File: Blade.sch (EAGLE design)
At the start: 162 parts, among them IC1 THN10-2411WIR, IC10 MCP6064-E/SL, IC2 MCP6064-E/SL, IC3 MCP6064-E/SL, IC4 MCP6064-E/SL, IC5 MAX488CSA, IC6 MOCD207MSOIC-8, IC7 MOCD207MSOIC-8, IC8 MOCD207MSOIC-8, IC9 MCP6064-E/SL, Q1 12MHz, U1 ADR366WAUJZ, U10 ADS1148QPWRQ1, U11 ADS1148QPWRQ1, U12 ADS1148QPWRQ1, U2 ADR366WAUJZ, U3 ADS1148QPWRQ1, U4 ADS1148QPWRQ1, U5 ADS1148QPWRQ1, U6 LT1528, U7 S70FL01GS, U8 S70FL01GS, U9 STM32F77XXXLQFP208, X1 D-SUB9-H5M09RA, X2 D-SUB15-H5M15RA, X3 USBPTH

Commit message: rerouting
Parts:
- added C52: 10n, rcl:C-EUC0805
- added R22: 100k, rcl:R-EU_R0805
- added R23: 1k, rcl:R-EU_R0805
- added R24, R25: ?, rcl:R-EU_R0805
- added U13: ADR366WAUJZ, ADR360:ADR36_UJZ
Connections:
- new net 3V3REF3: R24.2, U13.VOUT, U9.VREF+
- new net ADC4_DRDY: U11.!DRDY, U9.PH0
- new net ADC4_RES: U11.!RESET, U9.PF10
- new net ADC4_START: U11.START, U9.PF9
- new net ADC5_DRDY: U10.!DRDY, U9.PA1
- new net ADC5_RES: U10.!RESET, U9.PC2
- new net ADC5_START: U10.START, U9.PC0
- new net ADC6_DRDY: U12.!DRDY, U9.PA2
- new net ADC6_RES: U12.!RESET, U9.PH1
- new net ADC6_START: U12.START, U9.PC3
- new net N$68: R22.1, U13.TRIM
- new net N$69: R22.2, R24.1, R25.2
- new net N$70: R23.2, R25.1
- net 3V3REF2: no longer U9.VREF+
- net 5V: now also C52.2, U13.VIN
- net ADC1_DRDY: no longer U11.!DRDY
- net ADC1_RES: no longer U11.!RESET
- net ADC1_START: no longer U11.START
- net ADC2_DRDY: no longer U10.!DRDY
- net ADC2_RES: no longer U10.!RESET
- net ADC2_START: no longer U10.START
- net ADC3_DRDY: no longer U12.!DRDY
- net ADC3_RES: no longer U12.!RESET
- net ADC3_START: no longer U12.START
- net GND: now also C52.1, R23.1, U13.GND

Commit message: bom added, text cleanup
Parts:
- renumbered SV1 to X_PROG, U$1 to IC12, U$2 to IC13
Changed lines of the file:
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@@
 <part name="X1" library="con-thomas-betts" library_urn="urn:adsk.eagle:library:191" deviceset="D-SUB9-" device="H5M09RA" package3d_urn="urn:adsk.eagle:package:10559/1"/>
 <part name="X3" library="aSparkFun" deviceset="USB" device="PTH"/>
-<part name="SV1" library="con-lstb" library_urn="urn:adsk.eagle:library:162" deviceset="MA07-2" device="" package3d_urn="urn:adsk.eagle:package:8330/1"/>
-<part name="U$2" library="ch340g" deviceset="CH340G" device=""/>
+<part name="X_PROG" library="con-lstb" library_urn="urn:adsk.eagle:library:162" deviceset="MA07-2" device="" package3d_urn="urn:adsk.eagle:package:8330/1"/>
+<part name="IC13" library="ch340g" deviceset="CH340G" device=""/>
 <part name="Q1" library="adafruit" deviceset="CRYSTAL" device="SM49" value="12MHz"/>
 <part name="C1" library="rcl" deviceset="C-EU" device="C0603" value="22p"/>
@@
 <part name="D8" library="diodes" deviceset="DZ" device="MELF" value="3V6"/>
 <part name="D9" library="diodes" deviceset="DZ" device="MELF" value="3V6"/>
-<part name="U$1" library="m-pad-2.1" deviceset="LM78L05ACMX/NOPB" device=""/>
+<part name="IC12" library="m-pad-2.1" deviceset="LM78L05ACMX/NOPB" device=""/>
 <part name="C42" library="rcl" library_urn="urn:adsk.eagle:library:334" deviceset="C-EU" device="C0805" package3d_urn="urn:adsk.eagle:package:23617/2" value="100n"/>
 <part name="C43" library="rcl" library_urn="urn:adsk.eagle:library:334" deviceset="C-EU" device="C0805" package3d_urn="urn:adsk.eagle:package:23617/2" value="100n"/>
@@
 </instance>
 <instance part="X3" gate="G$1" x="101.6" y="93.98" smashed="yes" rot="R180"/>
-<instance part="SV1" gate="G$1" x="160.02" y="116.84" smashed="yes" rot="R180">
+<instance part="X_PROG" gate="G$1" x="160.02" y="116.84" smashed="yes" rot="R180">
 <attribute name="VALUE" x="163.83" y="129.54" size="1.778" layer="96" rot="R180"/>
 <attribute name="NAME" x="163.83" y="105.918" size="1.778" layer="95" rot="R180"/>
@@
 </segment>
 <segment>
-<pinref part="SV1" gate="G$1" pin="14"/>
+<pinref part="X_PROG" gate="G$1" pin="14"/>
 <wire x1="167.64" y1="109.22" x2="172.72" y2="109.22" width="0.1524" layer="91"/>
 <wire x1="172.72" y1="109.22" x2="172.72" y2="114.3" width="0.1524" layer="91"/>
-<pinref part="SV1" gate="G$1" pin="2"/>
+<pinref part="X_PROG" gate="G$1" pin="2"/>
 <wire x1="172.72" y1="114.3" x2="172.72" y2="116.84" width="0.1524" layer="91"/>
 <wire x1="172.72" y1="116.84" x2="172.72" y2="119.38" width="0.1524" layer="91"/>
@@
 <wire x1="172.72" y1="124.46" x2="167.64" y2="124.46" width="0.1524" layer="91"/>
 <label x="172.72" y="124.46" size="1.27" layer="95" xref="yes"/>
-<pinref part="SV1" gate="G$1" pin="4"/>
+<pinref part="X_PROG" gate="G$1" pin="4"/>
 <wire x1="167.64" y1="121.92" x2="172.72" y2="121.92" width="0.1524" layer="91"/>
 <junction x="172.72" y="121.92"/>
-<pinref part="SV1" gate="G$1" pin="6"/>
+<pinref part="X_PROG" gate="G$1" pin="6"/>
 <wire x1="172.72" y1="119.38" x2="167.64" y2="119.38" width="0.1524" layer="91"/>
 <junction x="172.72" y="119.38"/>
-<pinref part="SV1" gate="G$1" pin="8"/>
+<pinref part="X_PROG" gate="G$1" pin="8"/>
 <wire x1="167.64" y1="116.84" x2="172.72" y2="116.84" width="0.1524" layer="91"/>
 <junction x="172.72" y="116.84"/>
-<pinref part="SV1" gate="G$1" pin="10"/>
+<pinref part="X_PROG" gate="G$1" pin="10"/>
 <wire x1="167.64" y1="114.3" x2="172.72" y2="114.3" width="0.1524" layer="91"/>
 <junction x="172.72" y="114.3"/>
@@
 </segment>
 <segment>
-<pinref part="SV1" gate="G$1" pin="7"/>
+<pinref part="X_PROG" gate="G$1" pin="7"/>
 <wire x1="149.86" y1="116.84" x2="152.4" y2="116.84" width="0.1524" layer="91"/>
 <label x="149.86" y="116.84" size="1.27" layer="95" rot="R180" xref="yes"/>
@@
 </segment>
 <segment>
-<pinref part="SV1" gate="G$1" pin="9"/>
+<pinref part="X_PROG" gate="G$1" pin="9"/>
 <wire x1="149.86" y1="114.3" x2="152.4" y2="114.3" width="0.1524" layer="91"/>
 <label x="149.86" y="114.3" size="1.27" layer="95" rot="R180" xref="yes"/>
@@
 </segment>
 <segment>
-<pinref part="SV1" gate="G$1" pin="11"/>
+<pinref part="X_PROG" gate="G$1" pin="11"/>
 <wire x1="149.86" y1="111.76" x2="152.4" y2="111.76" width="0.1524" layer="91"/>
 <label x="149.86" y="111.76" size="1.27" layer="95" rot="R180" xref="yes"/>
@@
 </segment>
 <segment>
-<pinref part="SV1" gate="G$1" pin="3"/>
+<pinref part="X_PROG" gate="G$1" pin="3"/>
 <wire x1="149.86" y1="121.92" x2="152.4" y2="121.92" width="0.1524" layer="91"/>
 <label x="149.86" y="121.92" size="1.27" layer="95" rot="R180" xref="yes"/>
@@
 <net name="3V3" class="0">
 <segment>
-<pinref part="SV1" gate="G$1" pin="1"/>
+<pinref part="X_PROG" gate="G$1" pin="1"/>
 <wire x1="152.4" y1="124.46" x2="149.86" y2="124.46" width="0.1524" layer="91"/>
 <label x="149.86" y="124.46" size="1.27" layer="95" rot="R180" xref="yes"/>
@@
 <net name="TDI" class="0">
 <segment>
-<pinref part="SV1" gate="G$1" pin="5"/>
+<pinref part="X_PROG" gate="G$1" pin="5"/>
 <wire x1="149.86" y1="119.38" x2="152.4" y2="119.38" width="0.1524" layer="91"/>
 <label x="149.86" y="119.38" size="1.27" layer="95" rot="R180" xref="yes"/>
@@
 <net name="N$8" class="0">
 <segment>
-<pinref part="SV1" gate="G$1" pin="13"/>
+<pinref part="X_PROG" gate="G$1" pin="13"/>
 <wire x1="149.86" y1="109.22" x2="152.4" y2="109.22" width="0.1524" layer="91"/>
 </segment>
@@
 <net name="N$13" class="0">
 <segment>
-<pinref part="SV1" gate="G$1" pin="12"/>
+<pinref part="X_PROG" gate="G$1" pin="12"/>
 <wire x1="170.18" y1="111.76" x2="167.64" y2="111.76" width="0.1524" layer="91"/>
 </segment>
@@
 </plain>
 <instances>
-<instance part="U$2" gate="G$1" x="358.14" y="45.72" smashed="yes"/>
+<instance part="IC13" gate="G$1" x="358.14" y="45.72" smashed="yes"/>
 <instance part="Q1" gate="G$1" x="337.82" y="22.86" smashed="yes">
 <attribute name="NAME" x="340.36" y="23.876" size="1.778" layer="95"/>
@@
 <attribute name="VALUE" x="437.8325" y="267.335" size="1.524" layer="96" rot="R90"/>
 </instance>
-<instance part="U$1" gate="G$1" x="487.934" y="210.566" smashed="yes"/>
+<instance part="IC12" gate="G$1" x="487.934" y="210.566" smashed="yes"/>
 <instance part="C42" gate="G$1" x="480.314" y="192.786" smashed="yes" rot="R270">
 <attribute name="NAME" x="480.695" y="191.262" size="1.778" layer="95" rot="R270"/>
@@
 <net name="DAPI_P" class="0">
 <segment>
-<pinref part="U$2" gate="G$1" pin="D+"/>
+<pinref part="IC13" gate="G$1" pin="D+"/>
 <wire x1="345.44" y1="45.72" x2="312.42" y2="45.72" width="0.1524" layer="91"/>
 <label x="317.5" y="45.72" size="1.27" layer="95" rot="R270" xref="yes"/>
@@
 <net name="DAPI_N" class="0">
 <segment>
-<pinref part="U$2" gate="G$1" pin="D-"/>
+<pinref part="IC13" gate="G$1" pin="D-"/>
 <wire x1="345.44" y1="43.18" x2="322.58" y2="43.18" width="0.1524" layer="91"/>
 <label x="328.93" y="42.926" size="1.27" layer="95" rot="R270" xref="yes"/>
@@
 <net name="DAPI_RX" class="0">
 <segment>
-<pinref part="U$2" gate="G$1" pin="TX"/>
+<pinref part="IC13" gate="G$1" pin="TX"/>
 <label x="330.2" y="53.34" size="1.27" layer="95" rot="R90" xref="yes"/>
 <pinref part="D4" gate="G$1" pin="C"/>
@@
 <net name="GND" class="0">
 <segment>
-<pinref part="U$2" gate="G$1" pin="GND"/>
+<pinref part="IC13" gate="G$1" pin="GND"/>
 <wire x1="345.44" y1="55.88" x2="342.9" y2="55.88" width="0.1524" layer="91"/>
 <label x="342.9" y="55.88" size="1.27" layer="95" rot="R90" xref="yes"/>
@@
 <net name="3V3" class="0">
 <segment>
-<pinref part="U$2" gate="G$1" pin="VCC"/>
+<pinref part="IC13" gate="G$1" pin="VCC"/>
 <wire x1="370.84" y1="55.88" x2="373.38" y2="55.88" width="0.1524" layer="91"/>
 <label x="373.38" y="55.88" size="1.27" layer="95" rot="R90" xref="yes"/>
@@
 <segment>
 <pinref part="C2" gate="G$1" pin="1"/>
-<pinref part="U$2" gate="G$1" pin="XO"/>
+<pinref part="IC13" gate="G$1" pin="XO"/>
 <wire x1="345.44" y1="15.24" x2="345.44" y2="22.86" width="0.1524" layer="91"/>
 <pinref part="Q1" gate="G$1" pin="2"/>
@@
 <net name="N$3" class="0">
 <segment>
-<pinref part="U$2" gate="G$1" pin="XI"/>
+<pinref part="IC13" gate="G$1" pin="XI"/>
 <pinref part="C1" gate="G$1" pin="1"/>
 <wire x1="345.44" y1="40.64" x2="332.74" y2="40.64" width="0.1524" layer="91"/>
@@
 <segment>
 <pinref part="C42" gate="G$1" pin="2"/>
-<pinref part="U$1" gate="G$1" pin="VIN"/>
+<pinref part="IC12" gate="G$1" pin="VIN"/>
 <wire x1="475.234" y1="192.786" x2="475.234" y2="202.946" width="0.1524" layer="91"/>
 <label x="475.234" y="192.786" size="1.27" layer="95" rot="R180" xref="yes"/>
@@
 <pinref part="C43" gate="G$1" pin="2"/>
 <wire x1="482.854" y1="192.786" x2="487.934" y2="192.786" width="0.1524" layer="91"/>
-<pinref part="U$1" gate="G$1" pin="GND"/>
+<pinref part="IC12" gate="G$1" pin="GND"/>
 <wire x1="487.934" y1="192.786" x2="490.474" y2="192.786" width="0.1524" layer="91"/>
 <wire x1="487.934" y1="202.946" x2="487.934" y2="192.786" width="0.1524" layer="91"/>
@@
 <net name="DAPI_TX" class="0">
 <segment>
-<pinref part="U$2" gate="G$1" pin="RX"/>
+<pinref part="IC13" gate="G$1" pin="RX"/>
 <wire x1="345.44" y1="50.8" x2="304.8" y2="50.8" width="0.1524" layer="91"/>
 <label x="325.12" y="50.8" size="1.27" layer="95" rot="R90" xref="yes"/>
@@
 <pinref part="C43" gate="G$1" pin="1"/>
 <wire x1="498.094" y1="192.786" x2="500.634" y2="192.786" width="0.1524" layer="91"/>
-<pinref part="U$1" gate="G$1" pin="VOUT"/>
+<pinref part="IC12" gate="G$1" pin="VOUT"/>
 <wire x1="500.634" y1="192.786" x2="500.634" y2="202.946" width="0.1524" layer="91"/>
 <label x="500.634" y="192.786" size="1.27" layer="95" xref="yes"/>

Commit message: finished routing Rev. 1
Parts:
- D5, D6: value ~5V2 -> 6V
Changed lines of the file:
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@@
 <part name="IC5" library="maxim" library_urn="urn:adsk.eagle:library:269" deviceset="MAX488" device="CSA" package3d_urn="urn:adsk.eagle:package:17511/1"/>
 <part name="R10" library="rcl" deviceset="R-EU_" device="R0805" value="500"/>
-<part name="D5" library="diodes" deviceset="DZ" device="MELF" value="~5V2"/>
-<part name="D6" library="diodes" deviceset="DZ" device="MELF" value="~5V2"/>
+<part name="D5" library="diodes" deviceset="DZ" device="MELF" value="6V"/>
+<part name="D6" library="diodes" deviceset="DZ" device="MELF" value="6V"/>
 <part name="D7" library="diodes" deviceset="DZ" device="MELF" value="3V6"/>
 <part name="D8" library="diodes" deviceset="DZ" device="MELF" value="3V6"/>

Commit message: schematics png/pdf
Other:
- note added: "(5V-)28V rail 3V3 5V User LED 1 - 4"
- note added: "Filter/Buffer caps."
- note added: "Opto. isolation"
- note added: "RS422 driver"
- note added: "Spike protection"
- note added: "all logic sided on this page"
- note added: "logic side <-> RXSM side"
- note removed: "Galv. Trennung"
- note removed: "logic side"
- moved on the sheet: C1, C10, C11, C12, C13, C14, C15, C16, C17, C18, C19, C2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

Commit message: Werte Update
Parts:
- LED1, LED2, LED3, LED4, LED5, LED6: value (none) -> 1V9
- R18: value ? -> 330
- R19: value ? -> 150
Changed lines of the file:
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@@
 <?xml version="1.0" encoding="utf-8"?>
 <!DOCTYPE eagle SYSTEM "eagle.dtd">
-<eagle version="9.6.0">
+<eagle version="9.3.1">
 <drawing>
 <settings>
-<setting alwaysvectorfont="no"/>
+<setting alwaysvectorfont="yes"/>
 <setting verticaltext="up"/>
 </settings>
@@
 <part name="C14" library="rcl" library_urn="urn:adsk.eagle:library:334" deviceset="C-EU" device="C0805" package3d_urn="urn:adsk.eagle:package:23617/2" value="10u"/>
 <part name="C15" library="rcl" library_urn="urn:adsk.eagle:library:334" deviceset="CPOL-EU" device="153CLV-0810" package3d_urn="urn:adsk.eagle:package:23401/2" value="10u"/>
-<part name="LED1" library="adafruit" library_urn="urn:adsk.eagle:library:420" deviceset="LED" device="CHIP-LED0603" package3d_urn="urn:adsk.eagle:package:6240556/1"/>
-<part name="LED2" library="adafruit" library_urn="urn:adsk.eagle:library:420" deviceset="LED" device="CHIP-LED0603" package3d_urn="urn:adsk.eagle:package:6240556/1"/>
-<part name="LED3" library="adafruit" library_urn="urn:adsk.eagle:library:420" deviceset="LED" device="CHIP-LED0603" package3d_urn="urn:adsk.eagle:package:6240556/1"/>
-<part name="LED4" library="adafruit" library_urn="urn:adsk.eagle:library:420" deviceset="LED" device="CHIP-LED0603" package3d_urn="urn:adsk.eagle:package:6240556/1"/>
+<part name="LED1" library="adafruit" library_urn="urn:adsk.eagle:library:420" deviceset="LED" device="CHIP-LED0603" package3d_urn="urn:adsk.eagle:package:6240556/1" value="1V9"/>
+<part name="LED2" library="adafruit" library_urn="urn:adsk.eagle:library:420" deviceset="LED" device="CHIP-LED0603" package3d_urn="urn:adsk.eagle:package:6240556/1" value="1V9"/>
+<part name="LED3" library="adafruit" library_urn="urn:adsk.eagle:library:420" deviceset="LED" device="CHIP-LED0603" package3d_urn="urn:adsk.eagle:package:6240556/1" value="1V9"/>
+<part name="LED4" library="adafruit" library_urn="urn:adsk.eagle:library:420" deviceset="LED" device="CHIP-LED0603" package3d_urn="urn:adsk.eagle:package:6240556/1" value="1V9"/>
 <part name="RN10" library="resistor-dil" library_urn="urn:adsk.eagle:library:342" deviceset="4R-N" device="EXBS8V" package3d_urn="urn:adsk.eagle:package:24925/1" value="270"/>
 <part name="C16" library="rcl" library_urn="urn:adsk.eagle:library:334" deviceset="C-EU" device="C1206" package3d_urn="urn:adsk.eagle:package:23618/2" value="2.2u"/>
@@
 <part name="R16" library="rcl" deviceset="R-EU_" device="R0805" value="3k3"/>
 <part name="R17" library="rcl" deviceset="R-EU_" device="R0805" value="3k3"/>
-<part name="LED5" library="adafruit" library_urn="urn:adsk.eagle:library:420" deviceset="LED" device="CHIP-LED0603" package3d_urn="urn:adsk.eagle:package:6240556/1"/>
-<part name="LED6" library="adafruit" library_urn="urn:adsk.eagle:library:420" deviceset="LED" device="CHIP-LED0603" package3d_urn="urn:adsk.eagle:package:6240556/1"/>
-<part name="R18" library="rcl" library_urn="urn:adsk.eagle:library:334" deviceset="R-EU_" device="R0805" package3d_urn="urn:adsk.eagle:package:23553/2" value="?"/>
-<part name="R19" library="rcl" library_urn="urn:adsk.eagle:library:334" deviceset="R-EU_" device="R0805" package3d_urn="urn:adsk.eagle:package:23553/2" value="?"/>
+<part name="LED5" library="adafruit" library_urn="urn:adsk.eagle:library:420" deviceset="LED" device="CHIP-LED0603" package3d_urn="urn:adsk.eagle:package:6240556/1" value="1V9"/>
+<part name="LED6" library="adafruit" library_urn="urn:adsk.eagle:library:420" deviceset="LED" device="CHIP-LED0603" package3d_urn="urn:adsk.eagle:package:6240556/1" value="1V9"/>
+<part name="R18" library="rcl" library_urn="urn:adsk.eagle:library:334" deviceset="R-EU_" device="R0805" package3d_urn="urn:adsk.eagle:package:23553/2" value="330"/>
+<part name="R19" library="rcl" library_urn="urn:adsk.eagle:library:334" deviceset="R-EU_" device="R0805" package3d_urn="urn:adsk.eagle:package:23553/2" value="150"/>
 <part name="LED7" library="adafruit" library_urn="urn:adsk.eagle:library:420" deviceset="LED" device="CHIP-LED0603" package3d_urn="urn:adsk.eagle:package:6240556/1"/>
 <part name="R20" library="rcl" library_urn="urn:adsk.eagle:library:334" deviceset="R-EU_" device="R0805" package3d_urn="urn:adsk.eagle:package:23553/2" value="?"/>

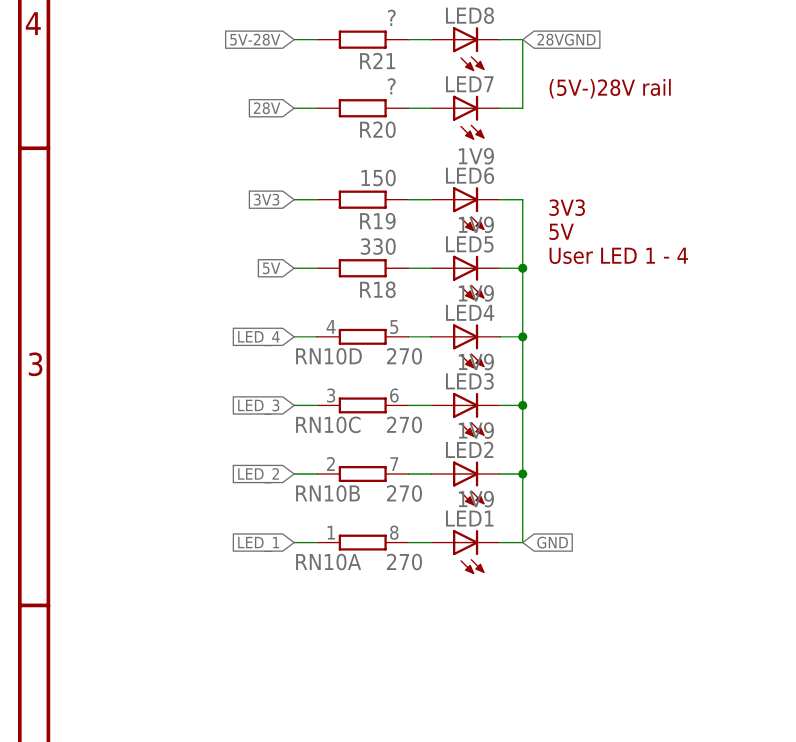
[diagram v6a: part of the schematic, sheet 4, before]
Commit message: led widerstand angepasst
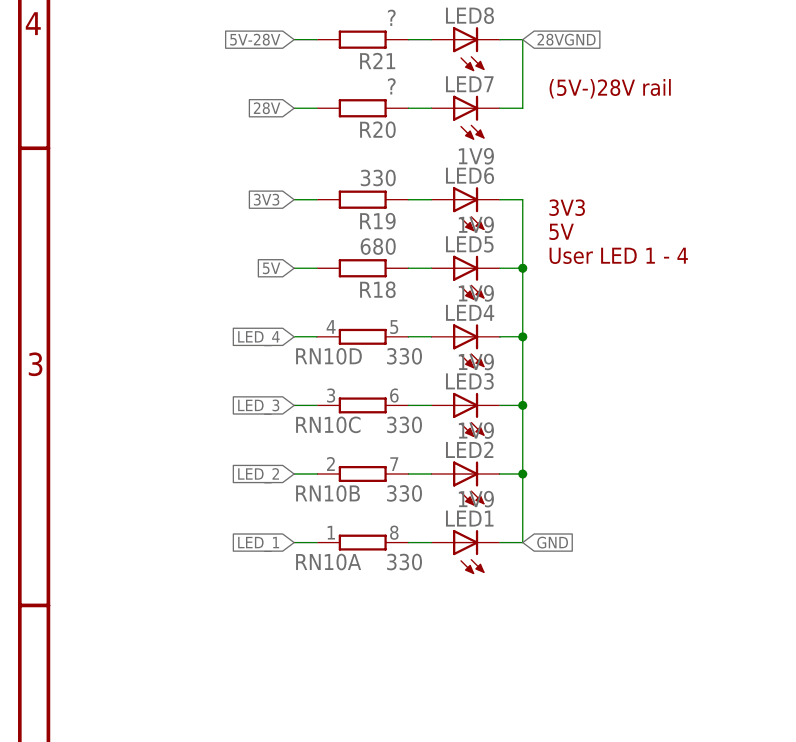
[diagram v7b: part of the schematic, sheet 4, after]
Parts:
- R18: value 330 -> 680
- R19: value 150 -> 330
- RN10: value 270 -> 330
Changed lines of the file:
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@@
 <part name="LED3" library="adafruit" library_urn="urn:adsk.eagle:library:420" deviceset="LED" device="CHIP-LED0603" package3d_urn="urn:adsk.eagle:package:6240556/1" value="1V9"/>
 <part name="LED4" library="adafruit" library_urn="urn:adsk.eagle:library:420" deviceset="LED" device="CHIP-LED0603" package3d_urn="urn:adsk.eagle:package:6240556/1" value="1V9"/>
-<part name="RN10" library="resistor-dil" library_urn="urn:adsk.eagle:library:342" deviceset="4R-N" device="EXBS8V" package3d_urn="urn:adsk.eagle:package:24925/1" value="270"/>
+<part name="RN10" library="resistor-dil" library_urn="urn:adsk.eagle:library:342" deviceset="4R-N" device="EXBS8V" package3d_urn="urn:adsk.eagle:package:24925/1" value="330"/>
 <part name="C16" library="rcl" library_urn="urn:adsk.eagle:library:334" deviceset="C-EU" device="C1206" package3d_urn="urn:adsk.eagle:package:23618/2" value="2.2u"/>
 <part name="C17" library="rcl" library_urn="urn:adsk.eagle:library:334" deviceset="C-EU" device="C1206" package3d_urn="urn:adsk.eagle:package:23618/2" value="2.2u"/>
@@
 <part name="LED5" library="adafruit" library_urn="urn:adsk.eagle:library:420" deviceset="LED" device="CHIP-LED0603" package3d_urn="urn:adsk.eagle:package:6240556/1" value="1V9"/>
 <part name="LED6" library="adafruit" library_urn="urn:adsk.eagle:library:420" deviceset="LED" device="CHIP-LED0603" package3d_urn="urn:adsk.eagle:package:6240556/1" value="1V9"/>
-<part name="R18" library="rcl" library_urn="urn:adsk.eagle:library:334" deviceset="R-EU_" device="R0805" package3d_urn="urn:adsk.eagle:package:23553/2" value="330"/>
-<part name="R19" library="rcl" library_urn="urn:adsk.eagle:library:334" deviceset="R-EU_" device="R0805" package3d_urn="urn:adsk.eagle:package:23553/2" value="150"/>
+<part name="R18" library="rcl" library_urn="urn:adsk.eagle:library:334" deviceset="R-EU_" device="R0805" package3d_urn="urn:adsk.eagle:package:23553/2" value="680"/>
+<part name="R19" library="rcl" library_urn="urn:adsk.eagle:library:334" deviceset="R-EU_" device="R0805" package3d_urn="urn:adsk.eagle:package:23553/2" value="330"/>
 <part name="LED7" library="adafruit" library_urn="urn:adsk.eagle:library:420" deviceset="LED" device="CHIP-LED0603" package3d_urn="urn:adsk.eagle:package:6240556/1"/>
 <part name="R20" library="rcl" library_urn="urn:adsk.eagle:library:334" deviceset="R-EU_" device="R0805" package3d_urn="urn:adsk.eagle:package:23553/2" value="?"/>
